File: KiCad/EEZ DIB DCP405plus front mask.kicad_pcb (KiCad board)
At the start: 2 copper layers, 35 x 111.5 mm, 1 part

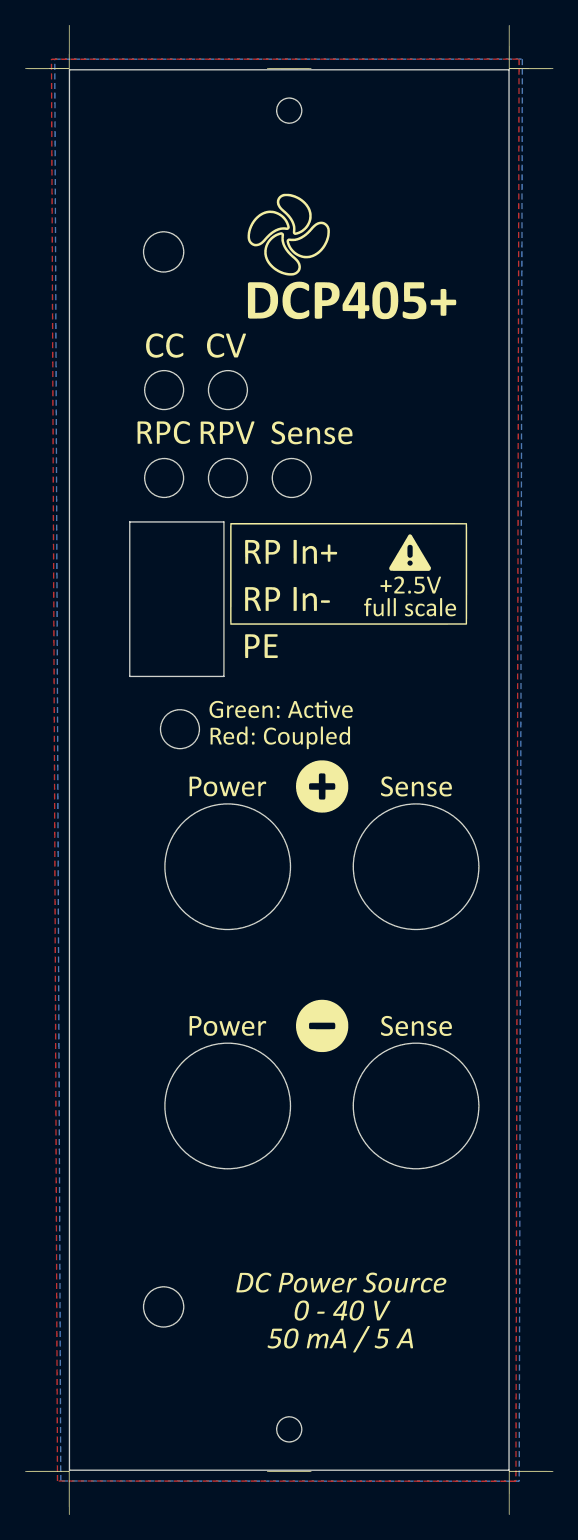
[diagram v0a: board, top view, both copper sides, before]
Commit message: Front mask mounting holes reinforcements
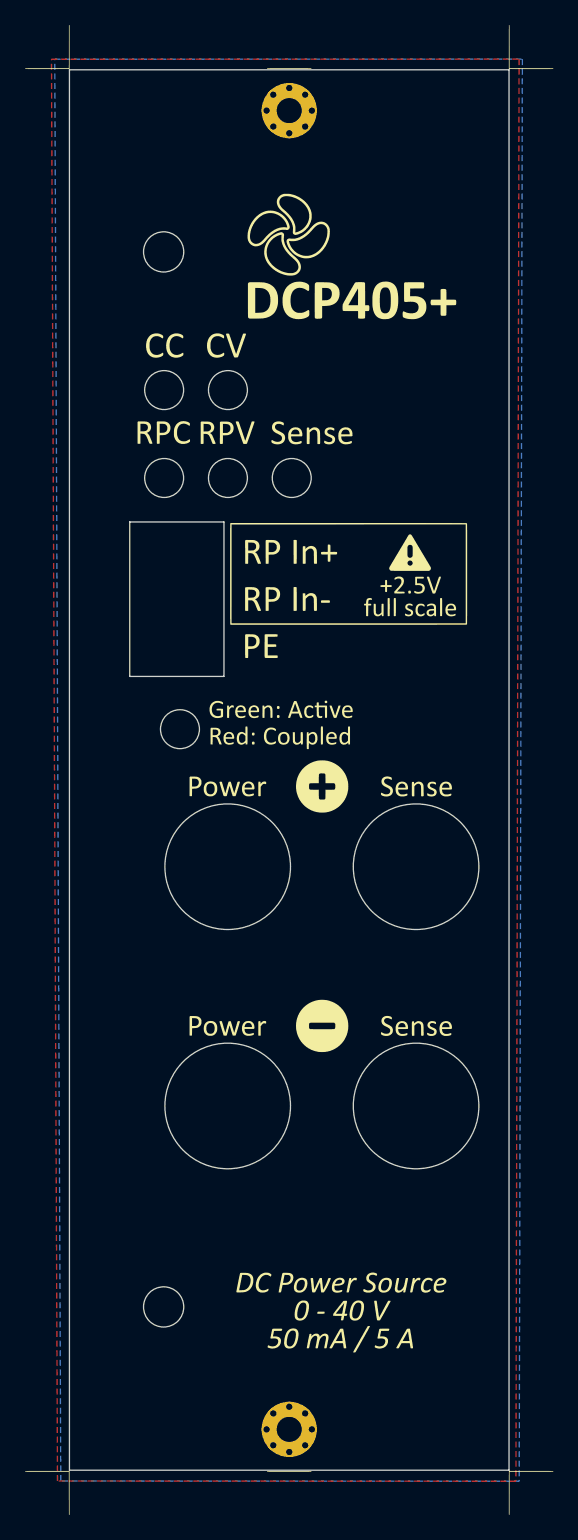
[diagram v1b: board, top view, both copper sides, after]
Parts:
- added REF**: MountingHole, PCM_EEZ_THT:Mounting_hole 2_4.4mm_via_NO_NET, F.Cu at (158.0, 146.8)
- added REF**: MountingHole, PCM_EEZ_THT:Mounting_hole 2_4.4mm_via_NO_NET, F.Cu at (158.0, 41.8)
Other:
- outline, holes or cut-outs redrawn
